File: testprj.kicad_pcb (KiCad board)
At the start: 4 copper layers, 286.5 x 81.5 mm, 104 parts, among them J10 AudioJack3_SwitchTR, J4 Conn_01x40_MountingPin, J7 AudioJack3_SwitchTR, J8 AudioJack3_SwitchTR, J9 AudioJack3_SwitchTR, SW1 SW_Push, SW10 SW_Push, SW11 SW_Push, SW12 SW_Push, SW13 SW_Push, SW14 SW_Push, SW15 SW_Push, SW16 SW_Push, SW17 SW_Push, SW18 SW_Push, SW19 SW_Push, SW2 SW_Push, SW20 SW_Push, SW3 SW_Push, SW4 SW_Push, SW5 SW_Push, SW6 SW_Push, SW7 SW_Push, SW8 SW_Push, SW9 SW_Push, U1 USBLC6-2SC6, U10 USBLC6-2SC6, U11 MCP3208, U12 SN74LVC1G125DBV, U13 74LVC1G32, U14 74LVC1G32, U15 ULN2002A, U16 ULN2002A, U17 ULN2002A, U18 ULN2002A, U2 ST1S10PHR, U3 LM4950TS, U4 74HC595, U5 W25Q128JVE, U6 74HC595, U7 74HC595, U8 74HC595, U9 USBLC6-2SC6, Y2 Crystal_GND24

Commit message: save state
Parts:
- moved R10 206.6 mm to (86.8, 136.0)
- moved R11 206.6 mm to (86.8, 138.9)
- moved R12 206.6 mm to (86.8, 141.9)
- moved R13 206.6 mm to (86.8, 144.8)
- moved C30 206.6 mm to (82.0, 136.0)
- moved C31 206.6 mm to (82.0, 139.0)
- moved C32 206.6 mm to (82.0, 142.0)
- moved C33 206.6 mm to (82.0, 145.0)
- moved U10 206.6 mm to (91.7, 141.5)
- moved U9 206.6 mm to (91.7, 136.9)
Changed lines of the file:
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@@
 	(footprint "Package_TO_SOT_SMD:SOT-23-6"
 		(layer "F.Cu")
-		(at 298.005 126.165)
+		(at 91.73 136.885)
 		(descr "SOT, 6 Pin (JEDEC MO-178 Var AB https://www.jedec.org/document_search?search_api_views_fulltext=MO-178)")
 		(tags "SOT TO_SOT_SMD")
@@
 	(footprint "Capacitor_SMD:C_0805_2012Metric_Pad1.18x1.45mm_HandSolder"
 		(layer "F.Cu")
-		(at 288.275 131.29)
+		(at 82 142.01)
 		(descr "Capacitor SMD 0805 (2012 Metric), square (rectangular) end terminal, IPC-7351 nominal with elongated pad for handsoldering. (Body size source: IPC-SM-782 page 76, https://www.pcb-3d.com/wordpress/wp-content/uploads/ipc-sm-782a_amendment_1_and_2.pdf, https://docs.google.com/spreadsheets/d/1BsfQQcO9C6DZCsRaXUlFlo91Tg2WpOkGARC1WS5S8t0/edit?usp=sharing)")
 		(tags "capacitor handsolder")
@@
 	(footprint "Capacitor_SMD:C_0805_2012Metric_Pad1.18x1.45mm_HandSolder"
 		(layer "F.Cu")
-		(at 288.275 125.27)
+		(at 82 135.99)
 		(descr "Capacitor SMD 0805 (2012 Metric), square (rectangular) end terminal, IPC-7351 nominal with elongated pad for handsoldering. (Body size source: IPC-SM-782 page 76, https://www.pcb-3d.com/wordpress/wp-content/uploads/ipc-sm-782a_amendment_1_and_2.pdf, https://docs.google.com/spreadsheets/d/1BsfQQcO9C6DZCsRaXUlFlo91Tg2WpOkGARC1WS5S8t0/edit?usp=sharing)")
 		(tags "capacitor handsolder")
@@
 	(footprint "Resistor_SMD:R_0805_2012Metric_Pad1.20x1.40mm_HandSolder"
 		(layer "F.Cu")
-		(at 293.055 125.24)
+		(at 86.78 135.96)
 		(descr "Resistor SMD 0805 (2012 Metric), square (rectangular) end terminal, IPC-7351 nominal with elongated pad for handsoldering. (Body size source: IPC-SM-782 page 72, https://www.pcb-3d.com/wordpress/wp-content/uploads/ipc-sm-782a_amendment_1_and_2.pdf)")
 		(tags "resistor handsolder")
@@
 	(footprint "Package_TO_SOT_SMD:SOT-23-6"
 		(layer "F.Cu")
-		(at 298.005 130.79)
+		(at 91.73 141.51)
 		(descr "SOT, 6 Pin (JEDEC MO-178 Var AB https://www.jedec.org/document_search?search_api_views_fulltext=MO-178)")
 		(tags "SOT TO_SOT_SMD")
@@
 	(footprint "Resistor_SMD:R_0805_2012Metric_Pad1.20x1.40mm_HandSolder"
 		(layer "F.Cu")
-		(at 293.055 131.14)
+		(at 86.78 141.86)
 		(descr "Resistor SMD 0805 (2012 Metric), square (rectangular) end terminal, IPC-7351 nominal with elongated pad for handsoldering. (Body size source: IPC-SM-782 page 72, https://www.pcb-3d.com/wordpress/wp-content/uploads/ipc-sm-782a_amendment_1_and_2.pdf)")
 		(tags "resistor handsolder")
@@
 	(footprint "Capacitor_SMD:C_0805_2012Metric_Pad1.18x1.45mm_HandSolder"
 		(layer "F.Cu")
-		(at 288.275 128.28)
+		(at 82 139)
 		(descr "Capacitor SMD 0805 (2012 Metric), square (rectangular) end terminal, IPC-7351 nominal with elongated pad for handsoldering. (Body size source: IPC-SM-782 page 76, https://www.pcb-3d.com/wordpress/wp-content/uploads/ipc-sm-782a_amendment_1_and_2.pdf, https://docs.google.com/spreadsheets/d/1BsfQQcO9C6DZCsRaXUlFlo91Tg2WpOkGARC1WS5S8t0/edit?usp=sharing)")
 		(tags "capacitor handsolder")
@@
 	(footprint "Capacitor_SMD:C_0805_2012Metric_Pad1.18x1.45mm_HandSolder"
 		(layer "F.Cu")
-		(at 288.275 134.3)
+		(at 82 145.02)
 		(descr "Capacitor SMD 0805 (2012 Metric), square (rectangular) end terminal, IPC-7351 nominal with elongated pad for handsoldering. (Body size source: IPC-SM-782 page 76, https://www.pcb-3d.com/wordpress/wp-content/uploads/ipc-sm-782a_amendment_1_and_2.pdf, https://docs.google.com/spreadsheets/d/1BsfQQcO9C6DZCsRaXUlFlo91Tg2WpOkGARC1WS5S8t0/edit?usp=sharing)")
 		(tags "capacitor handsolder")
@@
 	(footprint "Resistor_SMD:R_0805_2012Metric_Pad1.20x1.40mm_HandSolder"
 		(layer "F.Cu")
-		(at 293.055 134.09)
+		(at 86.78 144.81)
 		(descr "Resistor SMD 0805 (2012 Metric), square (rectangular) end terminal, IPC-7351 nominal with elongated pad for handsoldering. (Body size source: IPC-SM-782 page 72, https://www.pcb-3d.com/wordpress/wp-content/uploads/ipc-sm-782a_amendment_1_and_2.pdf)")
 		(tags "resistor handsolder")
@@
 	(footprint "Resistor_SMD:R_0805_2012Metric_Pad1.20x1.40mm_HandSolder"
 		(layer "F.Cu")
-		(at 293.055 128.19)
+		(at 86.78 138.91)
 		(descr "Resistor SMD 0805 (2012 Metric), square (rectangular) end terminal, IPC-7351 nominal with elongated pad for handsoldering. (Body size source: IPC-SM-782 page 72, https://www.pcb-3d.com/wordpress/wp-content/uploads/ipc-sm-782a_amendment_1_and_2.pdf)")
 		(tags "resistor handsolder")

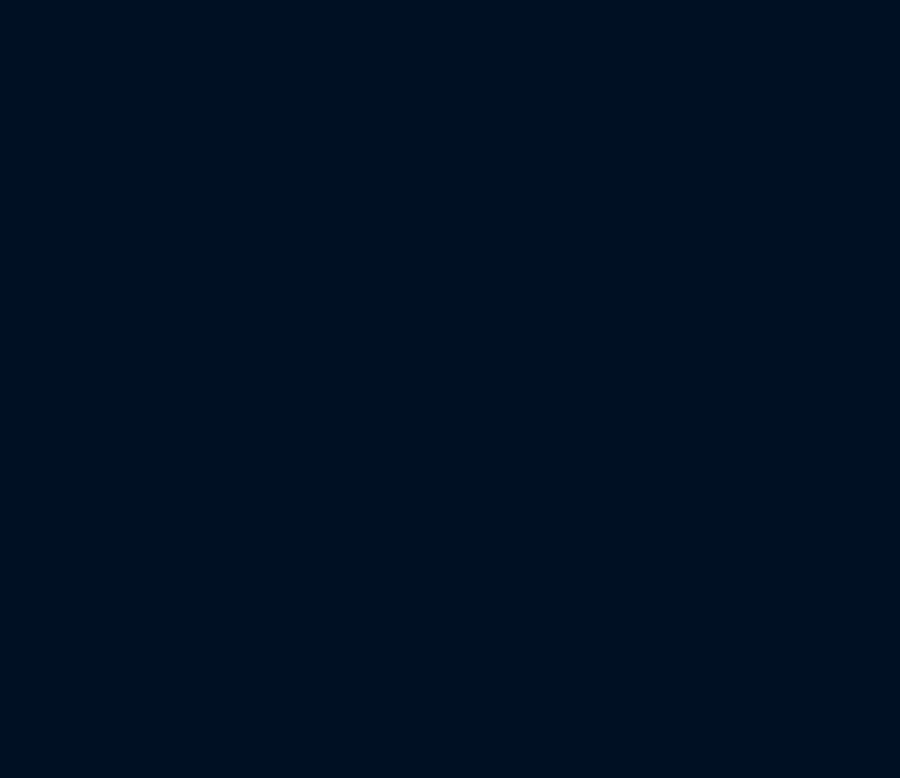
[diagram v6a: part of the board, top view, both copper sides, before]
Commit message: add lcd backlight chip
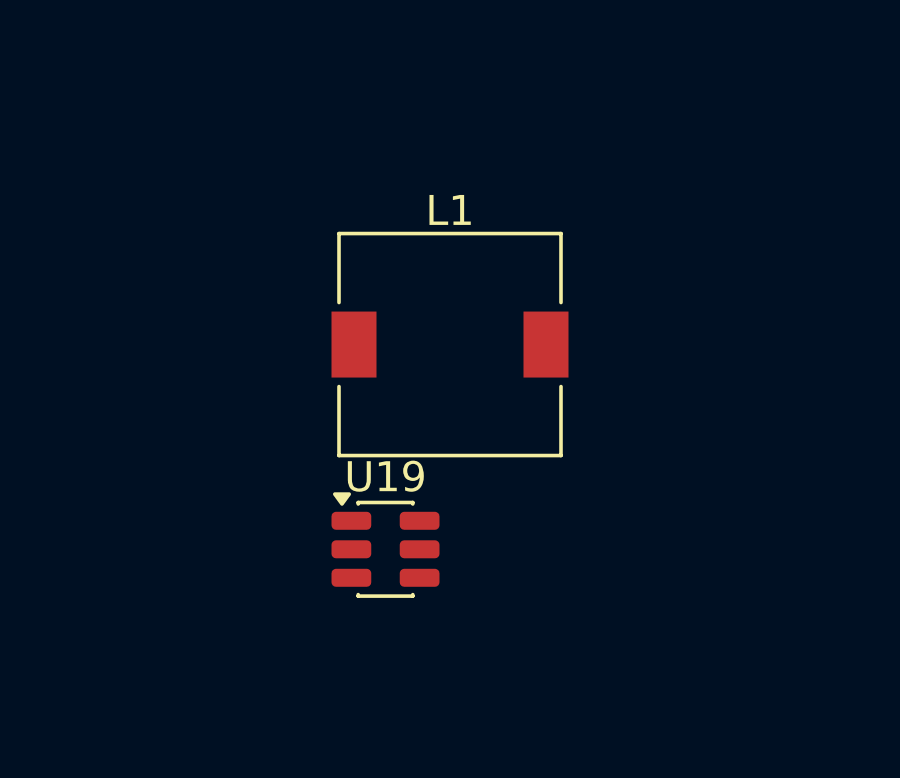
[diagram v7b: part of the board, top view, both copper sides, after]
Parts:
- added L1: L_Ferrite, Inductor_SMD:L_7.3x7.3_H4.5, F.Cu at (218.2, 107.4)
- added U19: AP3019AKTR, Package_TO_SOT_SMD:SOT-23-6, F.Cu at (216.1, 114.2)
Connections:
- J4 pad 1: unconnected-(J4-Pin_1-Pad1) -> /video/BL_CATODE
- J4 pad 2: unconnected-(J4-Pin_2-Pad2) -> /video/BL_ANODE
- J4 pad 31: VCC_3P3 -> DVDD1_3P3
- J4 pad 35: VCC_3P3 -> DVDD1_3P3
- J4 pad 4: VCC_3P3 -> DVDD1_3P3
- U15 pad 9: unconnected-(U15-COM-Pad9) -> DVDD1_12P0
- U16 pad 9: unconnected-(U16-COM-Pad9) -> DVDD1_12P0
- U17 pad 9: unconnected-(U17-COM-Pad9) -> DVDD1_12P0
- U18 pad 9: unconnected-(U18-COM-Pad9) -> DVDD1_12P0
